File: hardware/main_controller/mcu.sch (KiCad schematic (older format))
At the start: 3 parts

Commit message: Peripherals
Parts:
- added C?: C, symbol Device:C
- added R?: R, symbol Device:R
- added SW?: SW_Push, symbol Switch:SW_Push
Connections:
- net GND: now also C?.2, SW?.1
- net RESET: now also C?.1, R?.2, SW?.2
- new net +3V3: R?.1
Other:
- note added: "Reset Button"
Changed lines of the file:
@@
 S 700  700  850  250
 U 5FD5037D
-F0 "Port D" 50
-F1 "portd.sch" 50
+F0 "Port D/E" 50
+F1 "portde.sch" 50
 $EndSheet
 $Sheet
@@
 Wire Notes Line
 	5300 1450 5300 500
+$Comp
+L Switch:SW_Push SW?
+U 1 1 5FDADA32
+P 4150 1300
+F 0 "SW?" H 4150 1585 50  0000 C CNN
+F 1 "SW_Push" H 4150 1494 50  0000 C CNN
+F 2 "" H 4150 1500 50  0001 C CNN
+F 3 "~" H 4150 1500 50  0001 C CNN
+	1    4150 1300
+	1    0    0    -1
+$EndComp
+$Comp
+L Device:R R?
+U 1 1 5FDAEBDA
+P 4500 1050
+F 0 "R?" H 4570 1096 50  0000 L CNN
+F 1 "R" H 4570 1005 50  0000 L CNN
+F 2 "" V 4430 1050 50  0001 C CNN
+F 3 "~" H 4500 1050 50  0001 C CNN
+	1    4500 1050
+	1    0    0    -1
+$EndComp
+$Comp
+L Device:C C?
+U 1 1 5FDAF4B5
+P 4500 1550
+F 0 "C?" H 4615 1596 50  0000 L CNN
+F 1 "C" H 4615 1505 50  0000 L CNN
+F 2 "" H 4538 1400 50  0001 C CNN
+F 3 "~" H 4500 1550 50  0001 C CNN
+	1    4500 1550
+	1    0    0    -1
+$EndComp
+$Comp
+L power:+3V3 #PWR?
+U 1 1 5FDB11D7
+P 4500 850
+F 0 "#PWR?" H 4500 700 50  0001 C CNN
+F 1 "+3V3" H 4515 1023 50  0000 C CNN
+F 2 "" H 4500 850 50  0001 C CNN
+F 3 "" H 4500 850 50  0001 C CNN
+	1    4500 850
+	1    0    0    -1
+$EndComp
+$Comp
+L power:GND #PWR?
+U 1 1 5FDB17E5
+P 4500 1750
+F 0 "#PWR?" H 4500 1500 50  0001 C CNN
+F 1 "GND" H 4505 1577 50  0000 C CNN
+F 2 "" H 4500 1750 50  0001 C CNN
+F 3 "" H 4500 1750 50  0001 C CNN
+	1    4500 1750
+	1    0    0    -1
+$EndComp
+Wire Wire Line
+	4500 1200 4500 1300
+Wire Wire Line
+	4500 1300 4350 1300
+Wire Wire Line
+	4500 1300 4500 1400
+Connection ~ 4500 1300
+Wire Wire Line
+	4500 900  4500 850
+Wire Wire Line
+	4500 1750 4500 1700
+$Comp
+L power:GND #PWR?
+U 1 1 5FDB4F7C
+P 3850 1400
+F 0 "#PWR?" H 3850 1150 50  0001 C CNN
+F 1 "GND" H 3855 1227 50  0000 C CNN
+F 2 "" H 3850 1400 50  0001 C CNN
+F 3 "" H 3850 1400 50  0001 C CNN
+	1    3850 1400
+	1    0    0    -1
+$EndComp
+Wire Wire Line
+	3950 1300 3850 1300
+Wire Wire Line
+	3850 1300 3850 1400
+Wire Wire Line
+	4500 1300 4850 1300
+Text GLabel 4850 1300 2    50   Input ~ 0
+RESET
+Wire Notes Line
+	5200 500  3400 500
+Wire Notes Line
+	3400 500  3400 2000
+Wire Notes Line
+	3400 2000 5200 2000
+Wire Notes Line
+	5200 2000 5200 500
+Text Notes 3950 650  2    50   ~ 0
+Reset Button
 $EndSCHEMATC

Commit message: LEDs
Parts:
- added D1, D2, D3, D4, D5: LED, symbol Device:LED
- added R? (x5): 510, symbol Device:R
- C?: value C -> 100nF
- R?: value R -> 10k
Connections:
- net +3V3: now also D1.2 (A), D2.2 (A), D3.2 (A), D4.2 (A), D5.2 (A)
- net GND: now also R?.1
- new net: D3.1 (K), R?.1
- new net: D2.1 (K), R?.1
- new net: D1.1 (K), R?.1
- new net: D4.1 (K), R?.2
- new net: D5.1 (K), R?.2
- new net LED1: R?.2
- new net LED2: R?.2
- new net LED3: R?.2
- new net LED4: R?.1
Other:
- note added: "Status LEDs"
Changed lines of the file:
@@
 P 4500 1050
 F 0 "R?" H 4570 1096 50  0000 L CNN
-F 1 "R" H 4570 1005 50  0000 L CNN
+F 1 "10k" H 4570 1005 50  0000 L CNN
 F 2 "" V 4430 1050 50  0001 C CNN
 F 3 "~" H 4500 1050 50  0001 C CNN
@@
 P 4500 1550
 F 0 "C?" H 4615 1596 50  0000 L CNN
-F 1 "C" H 4615 1505 50  0000 L CNN
+F 1 "100nF" H 4615 1505 50  0000 L CNN
 F 2 "" H 4538 1400 50  0001 C CNN
 F 3 "~" H 4500 1550 50  0001 C CNN
@@
 Wire Notes Line
 	5200 2000 5200 500
-Text Notes 3950 650  2    50   ~ 0
+Text Notes 3950 600  2    50   ~ 0
 Reset Button
+$Comp
+L Device:R R?
+U 1 1 5FD05EF1
+P 7950 1500
+F 0 "R?" V 7743 1500 50  0000 C CNN
+F 1 "510" V 7834 1500 50  0000 C CNN
+F 2 "" V 7880 1500 50  0001 C CNN
+F 3 "~" H 7950 1500 50  0001 C CNN
+	1    7950 1500
+	0    1    1    0
+$EndComp
+$Comp
+L Device:R R?
+U 1 1 5FD06B2C
+P 7950 1200
+F 0 "R?" V 7743 1200 50  0000 C CNN
+F 1 "510" V 7834 1200 50  0000 C CNN
+F 2 "" V 7880 1200 50  0001 C CNN
+F 3 "~" H 7950 1200 50  0001 C CNN
+	1    7950 1200
+	0    1    1    0
+$EndComp
+$Comp
+L Device:R R?
+U 1 1 5FD07500
+P 7950 900
+F 0 "R?" V 7743 900 50  0000 C CNN
+F 1 "510" V 7834 900 50  0000 C CNN
+F 2 "" V 7880 900 50  0001 C CNN
+F 3 "~" H 7950 900 50  0001 C CNN
+	1    7950 900
+	0    1    1    0
+$EndComp
+$Comp
+L Device:LED D1
+U 1 1 5FD09803
+P 8350 900
+F 0 "D1" H 8343 1117 50  0000 C CNN
+F 1 "LED" H 8343 1026 50  0000 C CNN
+F 2 "" H 8350 900 50  0001 C CNN
+F 3 "~" H 8350 900 50  0001 C CNN
+	1    8350 900
+	1    0    0    -1
+$EndComp
+$Comp
+L Device:LED D2
+U 1 1 5FD09F90
+P 8350 1200
+F 0 "D2" H 8343 1417 50  0000 C CNN
+F 1 "LED" H 8343 1326 50  0000 C CNN
+F 2 "" H 8350 1200 50  0001 C CNN
+F 3 "~" H 8350 1200 50  0001 C CNN
+	1    8350 1200
+	1    0    0    -1
+$EndComp
+$Comp
+L Device:LED D3
+U 1 1 5FD0A5CB
+P 8350 1500
+F 0 "D3" H 8343 1717 50  0000 C CNN
+F 1 "LED" H 8343 1626 50  0000 C CNN
+F 2 "" H 8350 1500 50  0001 C CNN
+F 3 "~" H 8350 1500 50  0001 C CNN
+	1    8350 1500
+	1    0    0    -1
+$EndComp
+Wire Wire Line
+	8200 900  8100 900
+Wire Wire Line
+	8200 1200 8100 1200
+Wire Wire Line
+	8200 1500 8100 1500
+Wire Wire Line
+	7800 900  7700 900
+Wire Wire Line
+	7800 1200 7700 1200
+Wire Wire Line
+	7800 1500 7700 1500
+$Comp
+L power:+3V3 #PWR?
+U 1 1 5FD0C693
+P 8600 800
+F 0 "#PWR?" H 8600 650 50  0001 C CNN
+F 1 "+3V3" H 8615 973 50  0000 C CNN
+F 2 "" H 8600 800 50  0001 C CNN
+F 3 "" H 8600 800 50  0001 C CNN
+	1    8600 800
+	1    0    0    -1
+$EndComp
+Wire Wire Line
+	8600 800  8600 900
+Wire Wire Line
+	8600 900  8500 900
+Wire Wire Line
+	8600 900  8600 1200
+Wire Wire Line
+	8600 1200 8500 1200
+Connection ~ 8600 900
+Wire Wire Line
+	8600 1200 8600 1500
+Wire Wire Line
+	8600 1500 8500 1500
+Connection ~ 8600 1200
+Text GLabel 7700 900  0    50   Input ~ 0
+LED1
+Text GLabel 7700 1200 0    50   Input ~ 0
+LED2
+Text GLabel 7700 1500 0    50   Input ~ 0
+LED3
+$Comp
+L Device:LED D4
+U 1 1 5FD0EC82
+P 8850 900
+F 0 "D4" H 8843 645 50  0000 C CNN
+F 1 "LED" H 8843 736 50  0000 C CNN
+F 2 "" H 8850 900 50  0001 C CNN
+F 3 "~" H 8850 900 50  0001 C CNN
+	1    8850 900
+	-1   0    0    1
+$EndComp
+$Comp
+L Device:LED D5
+U 1 1 5FD0F902
+P 8850 1200
+F 0 "D5" H 8843 945 50  0000 C CNN
+F 1 "LED" H 8843 1036 50  0000 C CNN
+F 2 "" H 8850 1200 50  0001 C CNN
+F 3 "~" H 8850 1200 50  0001 C CNN
+	1    8850 1200
+	-1   0    0    1
+$EndComp
+Wire Wire Line
+	8700 900  8600 900
+Wire Wire Line
+	8700 1200 8600 1200
+$Comp
+L Device:R R?
+U 1 1 5FD112F0
+P 9250 900
+F 0 "R?" V 9043 900 50  0000 C CNN
+F 1 "510" V 9134 900 50  0000 C CNN
+F 2 "" V 9180 900 50  0001 C CNN
+F 3 "~" H 9250 900 50  0001 C CNN
+	1    9250 900
+	0    1    1    0
+$EndComp
+$Comp
+L Device:R R?
+U 1 1 5FD11F7A
+P 9250 1200
+F 0 "R?" V 9043 1200 50  0000 C CNN
+F 1 "510" V 9134 1200 50  0000 C CNN
+F 2 "" V 9180 1200 50  0001 C CNN
+F 3 "~" H 9250 1200 50  0001 C CNN
+	1    9250 1200
+	0    1    1    0
+$EndComp
+Wire Wire Line
+	9400 900  9500 900
+$Comp
+L power:GND #PWR?
+U 1 1 5FD13A0D
+P 9500 1400
+F 0 "#PWR?" H 9500 1150 50  0001 C CNN
+F 1 "GND" H 9505 1227 50  0000 C CNN
+F 2 "" H 9500 1400 50  0001 C CNN
+F 3 "" H 9500 1400 50  0001 C CNN
+	1    9500 1400
+	1    0    0    -1
+$EndComp
+Wire Wire Line
+	9100 900  9000 900
+Wire Wire Line
+	9000 1200 9100 1200
+Text GLabel 9500 900  2    50   Input ~ 0
+LED4
+Wire Wire Line
+	9400 1200 9500 1200
+Wire Wire Line
+	9500 1200 9500 1400
+Wire Notes Line
+	7250 500  9900 500
+Wire Notes Line
+	9900 500  9900 1650
+Wire Notes Line
+	9900 1650 7250 1650
+Wire Notes Line
+	7250 1650 7250 500
+Text Notes 7750 600  2    50   ~ 0
+Status LEDs
 $EndSCHEMATC

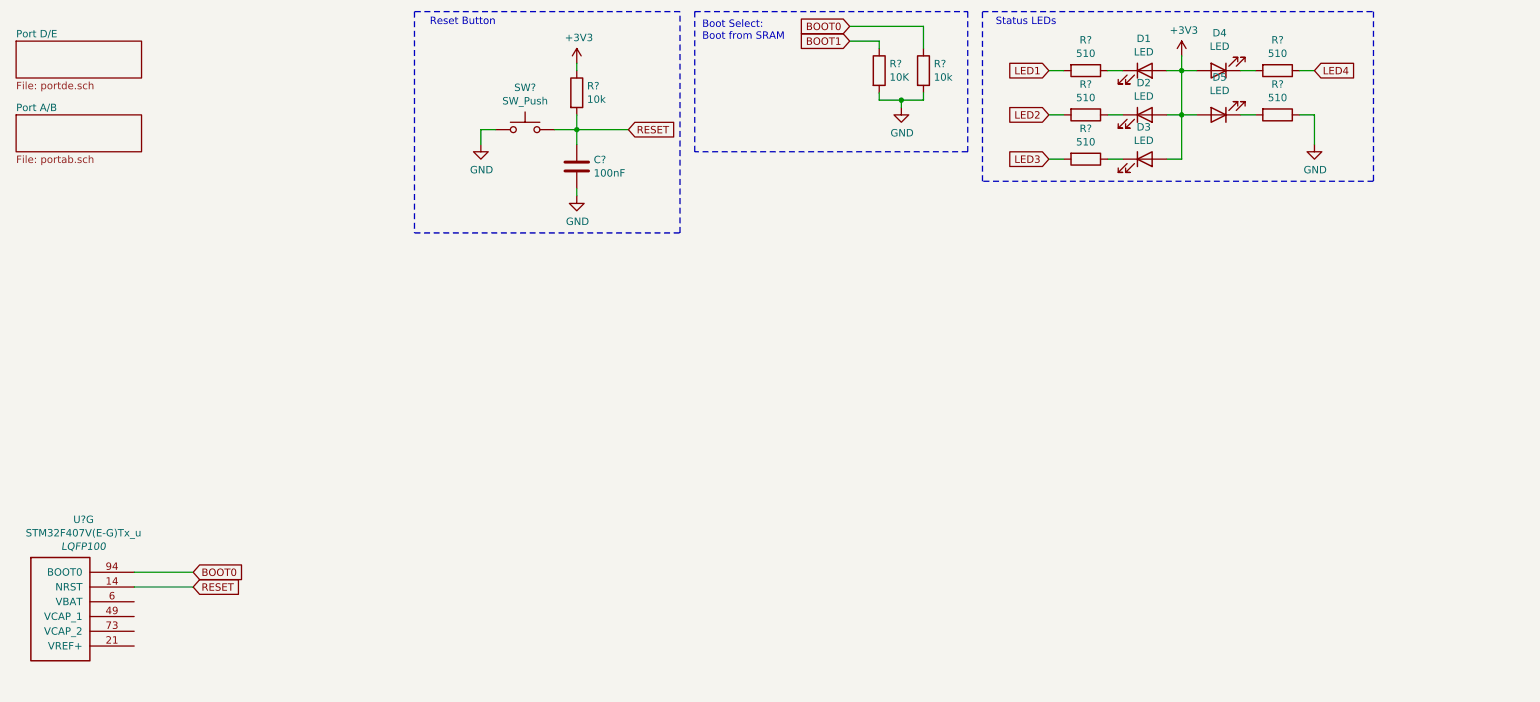
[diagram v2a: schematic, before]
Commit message: MCU Supply and Oscillator
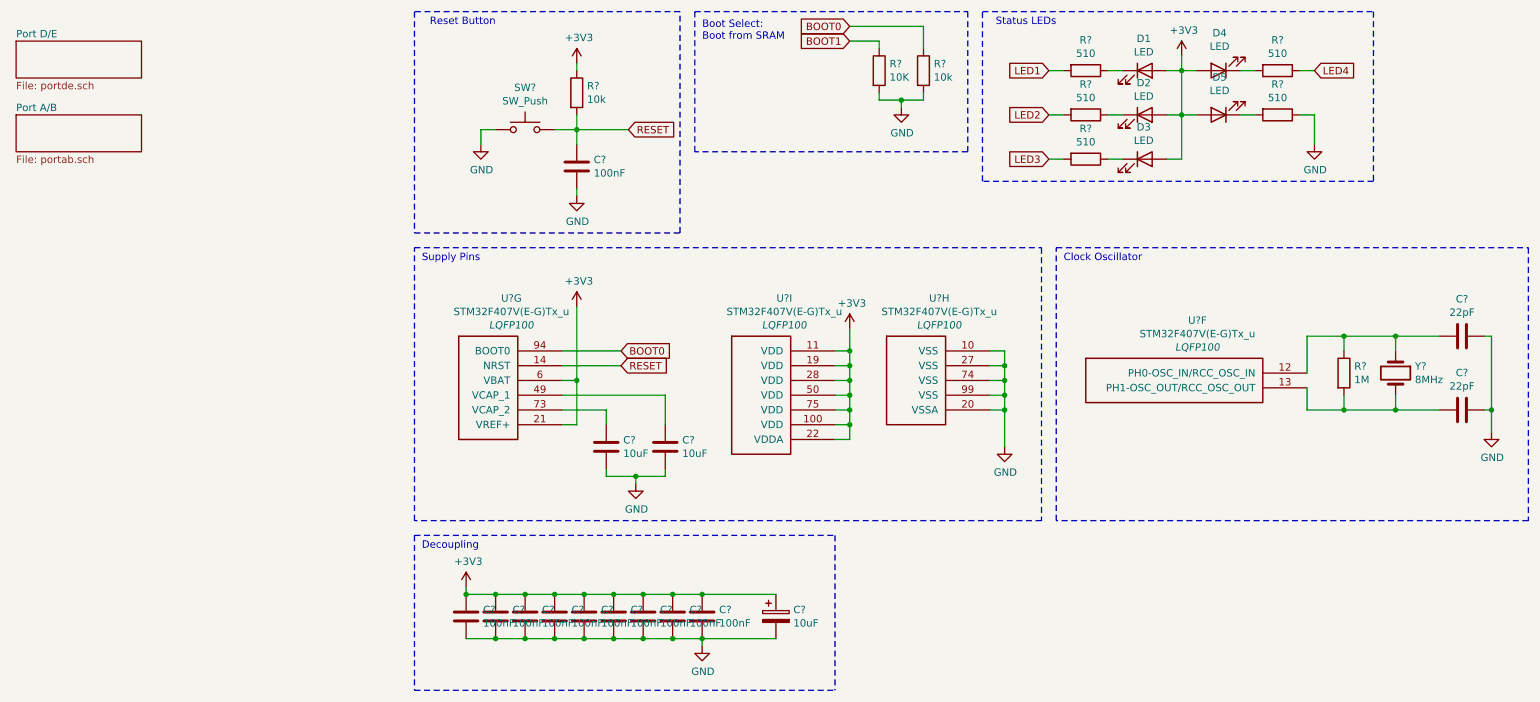
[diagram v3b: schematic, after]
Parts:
- added C? (x2): 10uF, symbol Device:C
- added C? (x9): 100nF, symbol Device:C
- added C?: 10uF, symbol Device:CP
- added C? (x2): 22pF, symbol Device:C
- added R?: 1M, symbol Device:R
- added U? (x3): STM32F407V(E-G)Tx_u, LQFP100, symbol stm32:STM32F407V(E-G)Tx_u
- added Y?: 8MHz, symbol Device:Crystal
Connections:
- net +3V3: now also U?.21 (VREF+), U?.6 (VBAT), C?.1, C?.1, C?.1, C?.1, C?.1, C?.1, C?.1, C?.1, C?.1, C?.1, U?.100 (VDD), U?.11 (VDD), U?.19 (VDD), U?.22 (VDDA), U?.28 (VDD), U?.50 (VDD), U?.75 (VDD)
- net GND: now also C?.1, C?.1, C?.2, C?.2, C?.2, C?.2, C?.2, C?.2, C?.2, C?.2, C?.2, C?.2, C?.2, C?.2, U?.10 (VSS), U?.20 (VSSA), U?.27 (VSS), U?.74 (VSS), U?.99 (VSS)
- net at U?.49 (VCAP_1): now also C?.1
- net at U?.73 (VCAP_2): now also C?.1
- new net: C?.2, R?.1, U?.12 (PH0-OSC_IN/RCC_OSC_IN), Y?.1
- new net: C?.2, R?.2, U?.13 (PH1-OSC_OUT/RCC_OSC_OUT), Y?.2
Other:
- note added: "Clock Oscillator"
- note added: "Decoupling"
- note added: "Supply Pins"
- moved on the sheet: U?G

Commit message: Assigned names
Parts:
- gave numbers to parts that had none: 27
